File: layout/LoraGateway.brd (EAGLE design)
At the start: 65 x 30 mm, 124 parts, among them J1 RPI-ZERO-HEADER, P2 LTST-C930KGKT, P3 LTST-C930KGKT, U1 SC283, U10 SE2435L, U2 SC560H, U6 SX1257, U7 SX1257, X1 USB2-MICRO, X3 END4825A, X4 END4263A, X5 SMA-KE11

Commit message: Rpi-shield
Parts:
- removed P3: LTST-C930KGKT, LoRa Gateway:LTST-C930KGKT
- removed R19, R22: 100, rcl:R0402
- added C12: 100nF, common:C0402
- added C13: 56pF, rcl:C0402
- added P1, P5, P6, P7, P8: LTST-C930KGKT, LoRa Gateway:LTST-C930KGKT
- added R10, R11, R7, R8, R9: 470, rcl:R0402
- added R3: EXB-N8V101JX, LoRa Gateway:EXB28V
- added R6: 100, rcl:R0402
- added U4: FGPMMOPA6H, LoRa Gateway:FGPMMOPA6H
- added X2: SMA-KE11, LoRa Gateway:J502-ND-142-0711-871/876
- C1, C2, C3, C4: device rcl:C1206 -> common:C1206
- C11, C23, C36, C5, C9: device rcl:C0805 -> common:C0805
- C24, C26, C27, C28, C29, C30, C31, C32, C33, C35, C39, C40, C41, C42, C43, C44, C48, C49, C50, C51, C52, C55, C56, C59, C60, C61, C62, C63, C64, C65, C66, C67, C68, C69, C70, C71, C72, C73, C74: device rcl:C0402 -> common:C0402
- C25, C34, C37, C38, C45, C46, C47, C53, C54, C58, C6: device rcl:C0603 -> common:C0603
- J1: value RPI-ZERO-HEADER -> RPI-HEADER3B; device LoRa Gateway:RPI-ZERO -> LoRa Gateway:RPI
- R16, R17: value 470 -> 100
- R18: value 100 -> 470
- moved L1 154.3 mm to (154.9, 65.7)
- moved C1 154.2 mm to (160.0, 64.0)
- moved U1 153.9 mm to (161.0, 68.0)
- moved C2 153.8 mm to (158.0, 68.0)
- moved C4 153.7 mm to (162.0, 72.0)
- moved C3 153.3 mm to (164.0, 68.0)
- moved L2 152.9 mm to (167.3, 70.3)
- moved P2 138.1 mm to (1.00, -28.0), turned to 0 degrees
- moved R18 123.6 mm to (-1.00, -22.0)
- moved C6 89.8 mm to (142.0, 74.0)
- moved C9 89.3 mm to (142.0, 76.0)
- moved C11 89.3 mm to (142.0, 72.0)
- moved U2 88.6 mm to (145.0, 74.0)
- moved C8 88.6 mm to (147.0, 74.0)
- moved R4 88.5 mm to (148.0, 74.0)
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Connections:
- removed net CLKO_B_32M: R22.2
- removed net GPIO0: U5.58
- removed net GPIO2: U5.56
- removed net GPIO3: U5.55
- removed net N$15 (its old number): P3.1, R17.2
- new net 3V3@1: J1.1
- new net N$10: R3.8, U5.2
- new net N$11: R3.7, U5.3
- new net N$33: R3.5, U5.5
- new net N$42: P1.1, R7.2
- new net N$5: R6.1, U5.39
- new net N$51: U4.11, X2.1
- new net N$66: P6.1, R9.2
- new net N$68: P7.1, R10.2
- new net N$69: P8.1, R11.2
- new net N$7: R11.1, U5.58
- new net N$71: R8.1, U5.55
- new net N$72: R18.2, U4.5
- new net N$73: U4.9
- new net N$74: U4.10
- new net N$75: C12.1, U4.1, U4.2
- new net N$76: P2.1, R18.1
- new net N$8: R9.1, U5.56
- net +5V: now also J1.2, J1.4
- net CLKI: now also R6.2; no longer R18.2
- net CLKO_B: now also R17.2; no longer R19.2, R22.1
- net FEM_EN: now also R16.2; no longer U3.2
- net GND: now also C12.2, C13.2, J1.14, J1.20, J1.25, J1.30, J1.34, J1.39, J1.6, J1.9, P1.2, P5.2, P6.2, P7.2, P8.2, U10.19, U4.12, U4.19, U4.3, U4.8, X2.G@1, X2.G@2, X2.G@3, X2.G@4; no longer P3.2
- net N$12: now also U3.2
- net N$14: now also R3.6, U5.4; no longer P2.1, R16.2
- net N$45: now also P5.1, R8.2; no longer R18.1, U5.39
- net N$58: now also R17.1; no longer R19.1
- net PPS: now also J1.18, U4.13
- net RADIO_RST: now also U5.25
- net RESET: now also J1.22
- net RX_ON: now also R10.1; no longer R17.1
- net SPI_MISO: now also J1.21, R3.2; no longer U5.3
- net SPI_MOSI: now also J1.19, R3.3; no longer U5.4
- net SPI_NSS: now also J1.24, R3.4; no longer U5.5
- net SPI_SCK: now also J1.23, R3.1; no longer U5.2
- net TX_ON: now also R7.1; no longer R16.1
- net VCCINT: now also C13.1, R16.1
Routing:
- net GND: track 0.00 -> 51.0 mm
- net VCCA_B: track 0.00 -> 4.55 mm
- net +5V: track 0.00 -> 4.01 mm
- net N$55: track 0.00 -> 1.70 mm
- net N$54: track 0.00 -> 1.70 mm
- net N$56: track 0.00 -> 1.68 mm
- net N$49: track 0.00 -> 1.45 mm
- net N$32: track 0.00 -> 1.00 mm
- added copper zone on layer 2, net GND
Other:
- board size 65 x 30 mm -> 65 x 56.5 mm

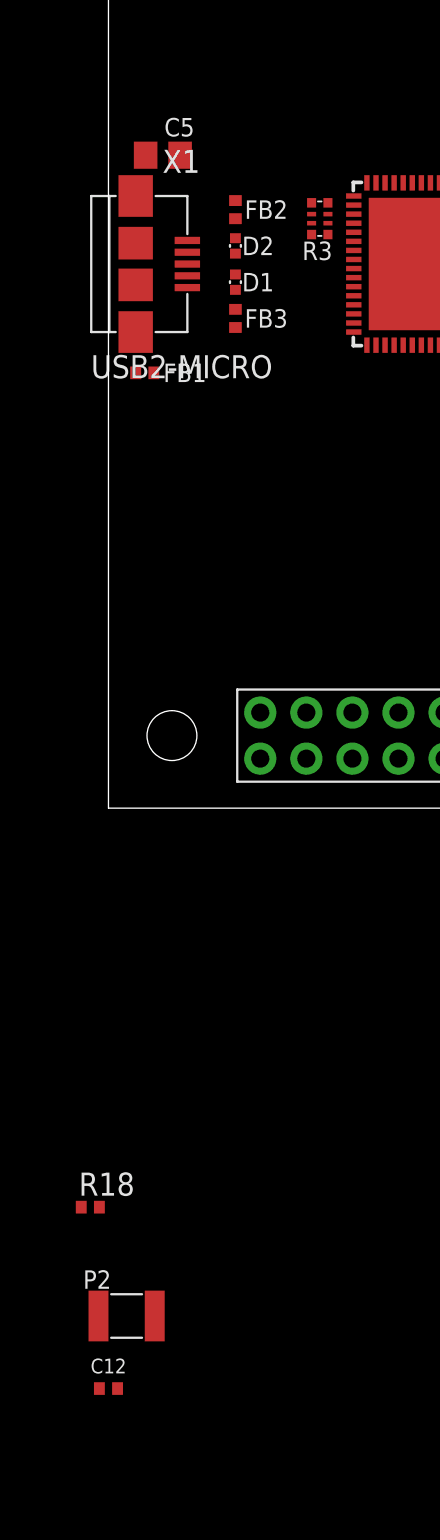
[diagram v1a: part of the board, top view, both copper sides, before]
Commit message: gps modul connected
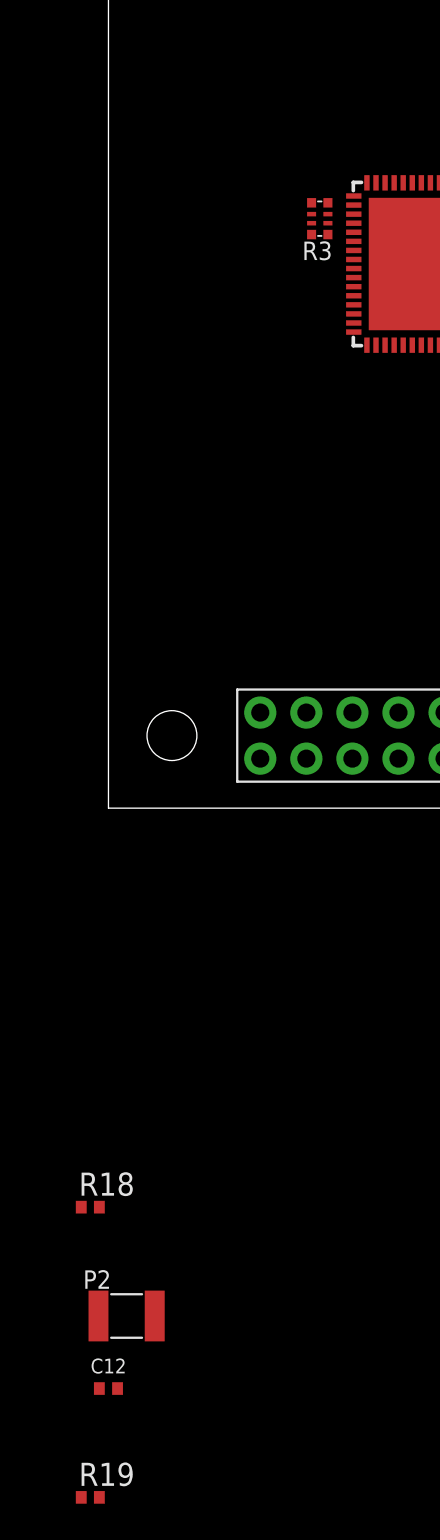
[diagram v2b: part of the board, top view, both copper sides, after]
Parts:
- removed C5: 1µF, common:C0805
- removed D1, D2: RCLAMP0531T, LoRa Gateway:SLP1006P2T
- removed FB1, FB2, FB3: (no value), LoRa Gateway:L0402
- removed X1: USB2-MICRO, LoRa Gateway:USB-2-MICRO
- added R19: 0, rcl:R0402
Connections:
- removed net N$6: D1.1, FB3.1, X1.5
- removed net N$73: U4.9
- removed net N$74: U4.10
- removed net N$9: FB1.2, X1.6, X1.7, X1.8, X1.9
- removed net VBUS: D2.1, FB2.1, X1.1
- new net 3V3@2: J1.17
- new net GPSRX: J1.8, U4.10
- new net GPSTX: J1.10, U4.9
- net +5V: no longer C5.2, FB2.2
- net GND: now also R19.1; no longer C5.1, D1.2, D2.2, FB1.1, FB3.2
- net N$75: now also R19.2

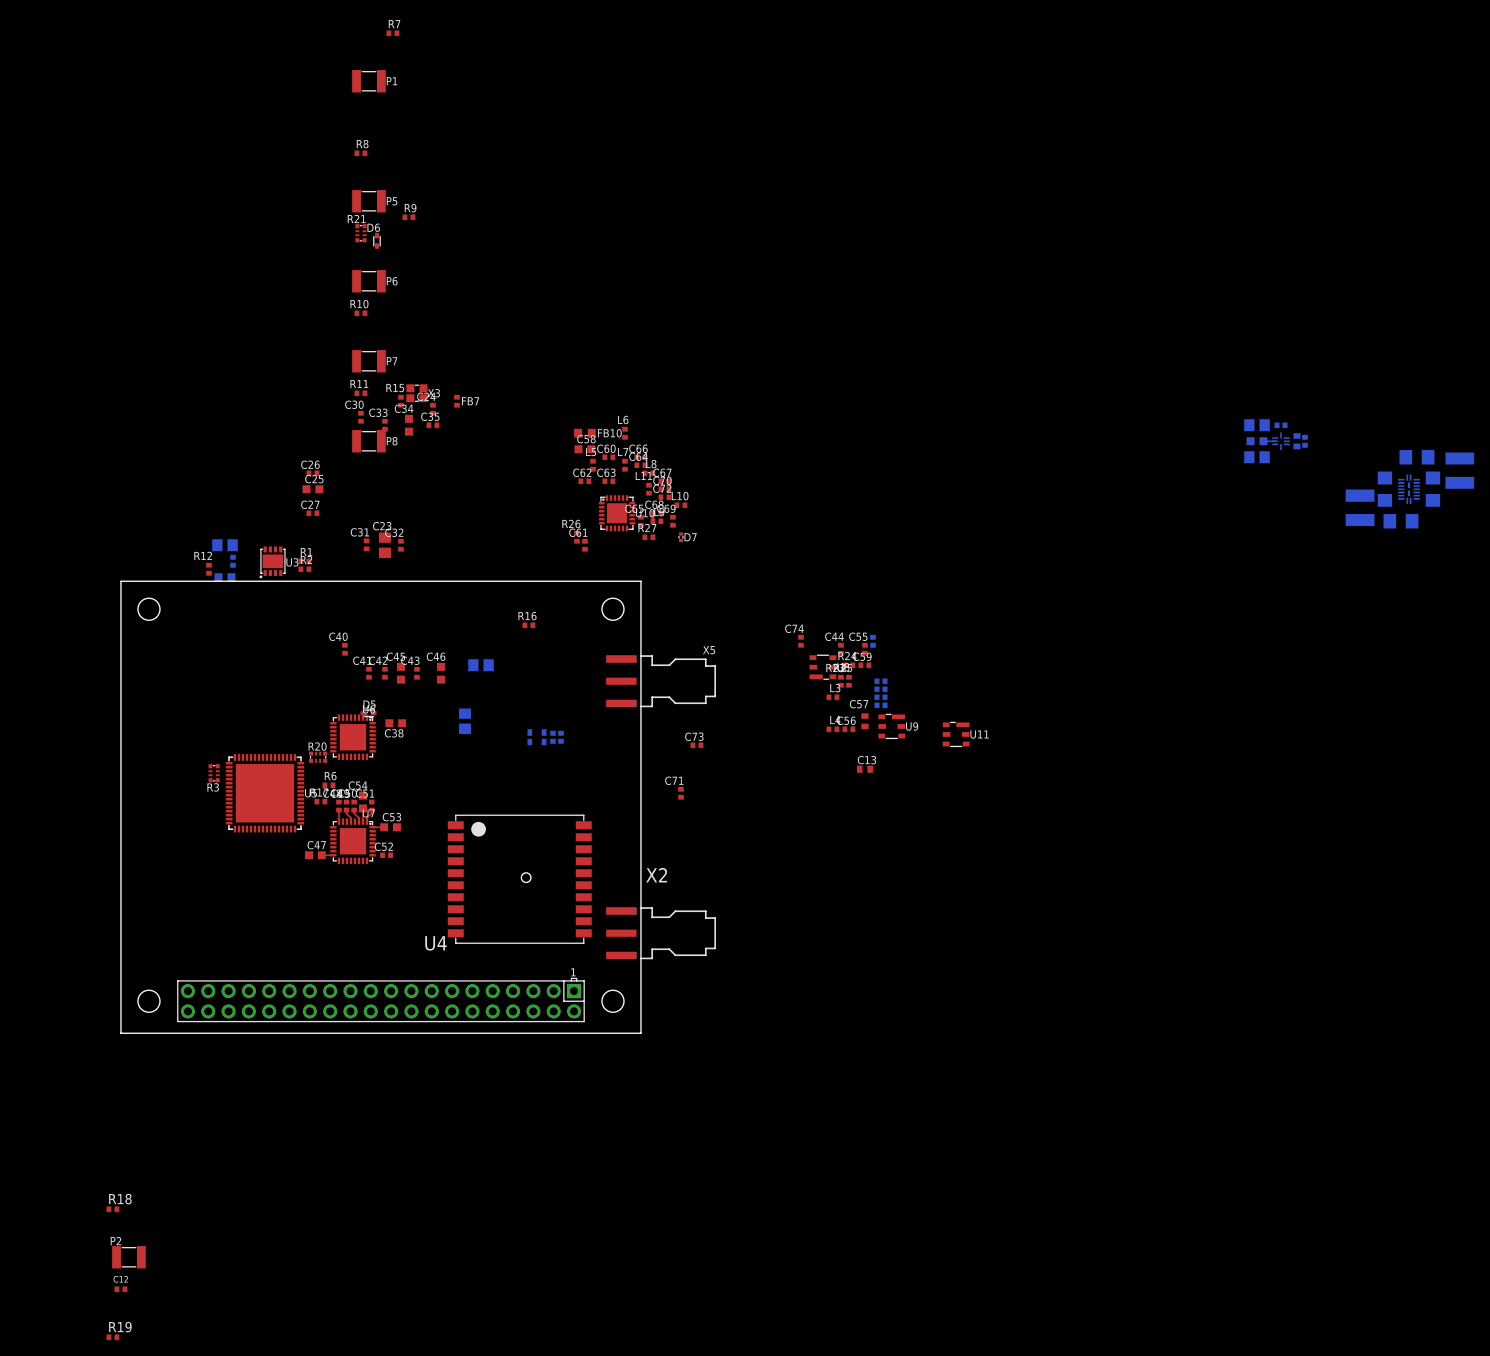
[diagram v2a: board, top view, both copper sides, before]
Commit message: gateway routed
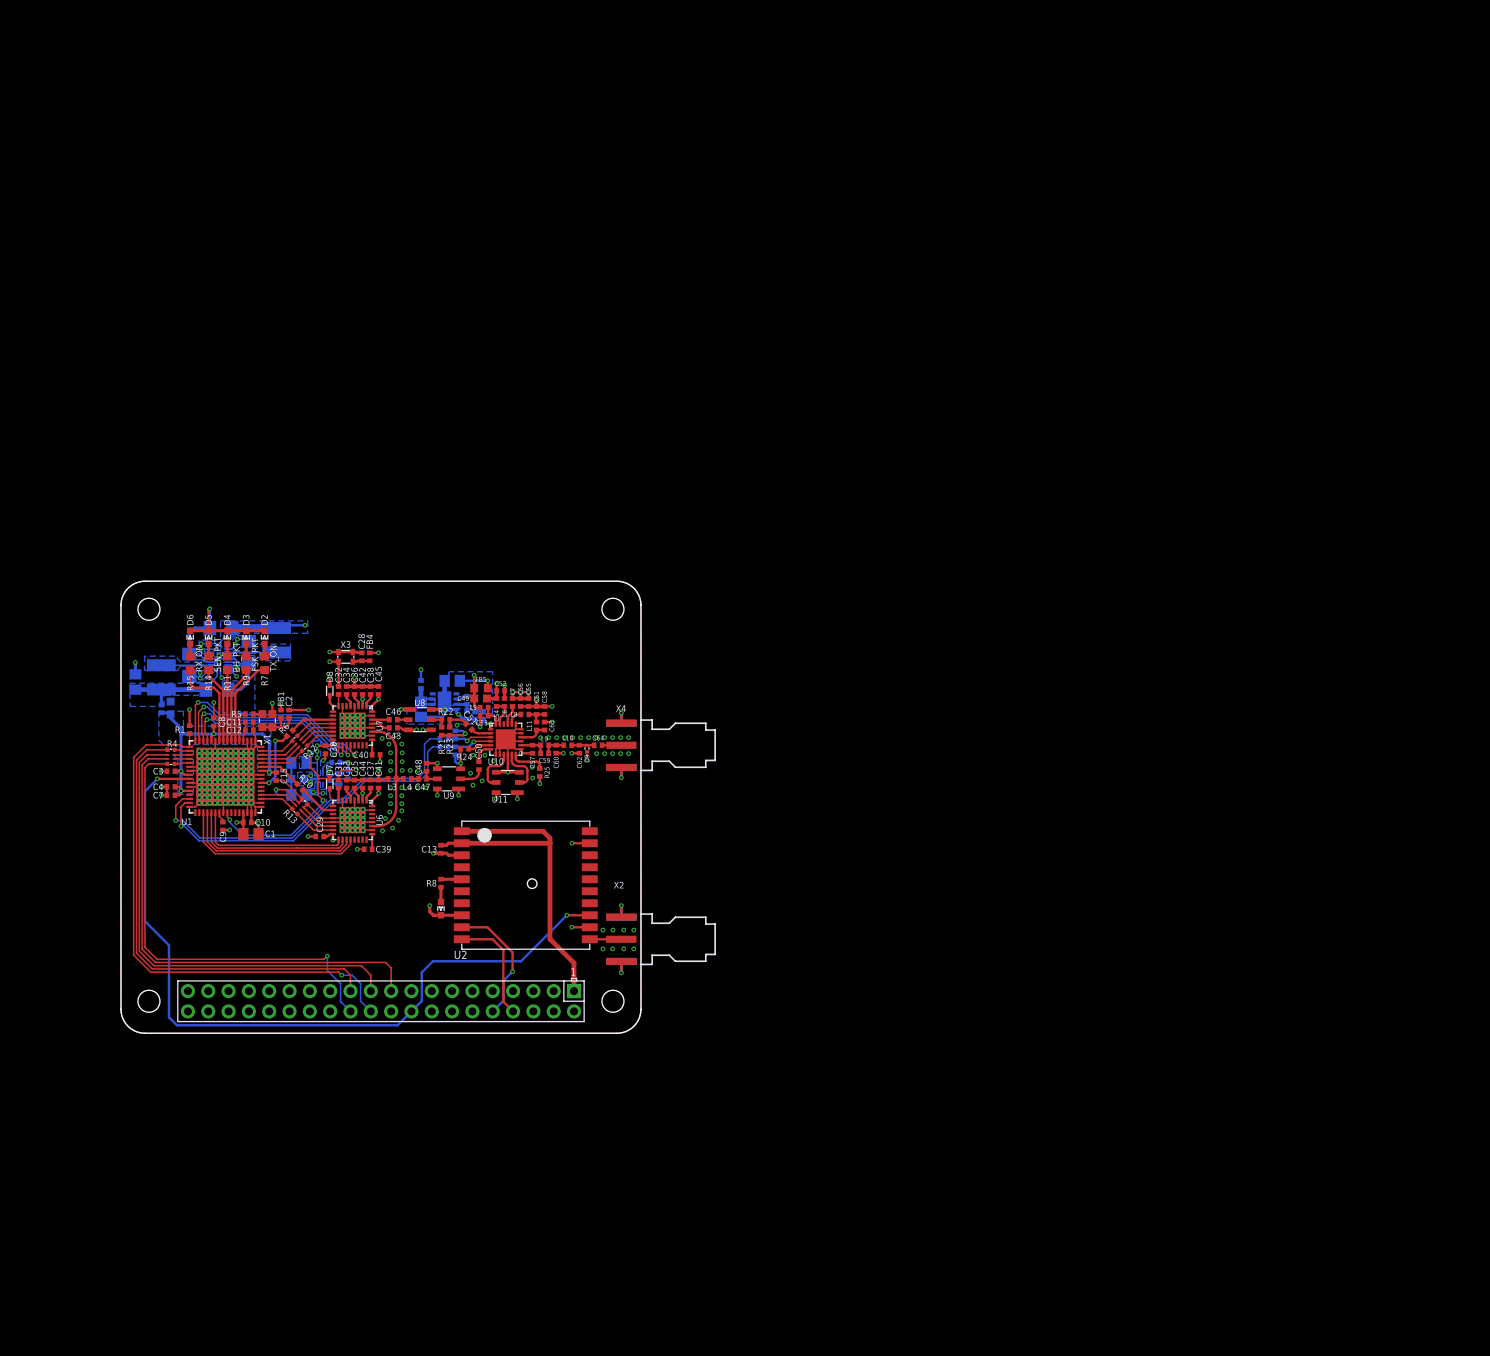
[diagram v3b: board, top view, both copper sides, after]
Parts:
- removed C65, C69: 3.3pF, common:C0402
- removed C66: 33pF, common:C0402
- removed C67: 7.5pF, common:C0402
- removed C68: 1.5pF, common:C0402
- removed C70, C72: 5.1pF, common:C0402
- removed C71: 2.7pF, common:C0402
- removed C73: 56pF, common:C0402
- removed C74: 100nF, common:C0402
- removed FB10: (no value), LoRa Gateway:L0603
- removed FB7, FB8, FB9: (no value), LoRa Gateway:L0402
- removed P1, P2, P5, P6, P7, P8: LTST-C930KGKT, LoRa Gateway:LTST-C930KGKT
- removed R26, R27: 49R9, rcl:R0402
- removed X5: SMA-KE11, LoRa Gateway:J502-ND-142-0711-871/876
- added C14: 10µF, common:C0805
- added C15: 100nF, common:C0402
- added C16: 1µF, common:C0603
- added C17, C21: 10uF, common:C0805
- added C18: 22uF, common:C1206
- added C19: 2.2uF, common:C0603
- added C20: 10uF, common:C1206
- added C22, C5: 56pF, common:C0402
- added D1, D2, D3, D4: LED, common:D0603
- added D8: BAT54XV2T1G, LoRa Gateway:SOD523
- added D9: LXES15AAA1-153, LoRa Gateway:LXES15AAA1-153
- added FB1, FB2, FB3: (no value), LoRa Gateway:L0402
- added FB5: (no value), LoRa Gateway:L0603
- added R22: 18, common:R0402
- added X1: END4825A, LoRa Gateway:2.5X2.0MM
- C1: value 22uF -> 10µF; device common:C1206 -> common:C0805
- C10, C7: value 10uF -> 100nF; device rcl:C0805 -> common:C0402
- C11, C9: value 1uF -> 100nF; device common:C0805 -> common:C0402
- C12, C30, C41, C42: value 100nF -> 1µF
- C13: value 56pF -> 100nF; device rcl:C0402 -> common:C0402
- C2: value 10uF -> 10nF; device common:C1206 -> common:C0402
- C23: value 10µF -> 10uF; device common:C0805 -> common:C1206
- C24: value 10nF -> 100nF; device common:C0402 -> rcl:C0402
- C25: value 1µF -> 1uF; device common:C0603 -> common:C0805
- C26: value 100nF -> 22uF; device common:C0402 -> common:C1206
- C27: value 100nF -> 1uF; device common:C0402 -> common:C0805
- C28: value 56pF -> 100nF
- C29, C44: value 56pF -> 1µF
- C3: value 10uF -> 1µF; device common:C1206 -> common:C0402
- C31, C32: value 100nF -> 1nF
- C34: value 1µF -> 100nF; device common:C0603 -> common:C0402
- C36: value 10µF -> 100nF; device common:C0805 -> common:C0402
- C37, C38: value 1µF -> 10nF; device common:C0603 -> common:C0402
- C4: value 22uF -> 100nF; device common:C1206 -> common:C0402
- C40: value 1nF -> 100nF
- C43: value 10nF -> 56pF
- C45: device common:C0603 -> common:C0402
- C46, C47: value 1µF -> 56pF; device common:C0603 -> common:C0402
- C48: value 1nF -> 5.6pF
- C49: value 100nF -> 4.7µF; device common:C0402 -> common:C0603
- C50: value 100nF -> 56pF
- C51, C60: value 10nF -> 3.3pF
- C52: value 100nF -> 10nF
- C53: value 1µF -> 150pF; device common:C0603 -> common:C0402
- C54: value 1µF -> 22pF; device common:C0603 -> common:C0402
- C55: value 56pF -> 1nF
- C56: value 56pF -> 33pF
- C57: value 5.6pF -> 3.3pF; device rcl:C0402 -> common:C0402
- C58: value 4.7µF -> 7.5pF; device common:C0603 -> common:C0402
- C59: value 3.3pF -> 1.5pF
- C6: value 2.2uF -> 56pF; device common:C0603 -> common:C0402
- C61: value 56pF -> 5.1pF
- C62: value 150pF -> 2.7pF
- C63: value 22pF -> 5.1pF
- C64: value 1nF -> 56pF
- C8: device rcl:C0402 -> common:C0402
- D5, D6: value BAT54XV2T1G -> LED; device LoRa Gateway:SOD523 -> common:D0603
- D7: value LXES15AAA1-153 -> BAT54XV2T1G; device LoRa Gateway:LXES15AAA1-153 -> LoRa Gateway:SOD523
- L10, L11, L3, L4, L5, L6, L7, L8, L9: device LoRa Gateway:L0402 -> common:L0402
- R1: value 16k -> 10k
- R10: value 470 -> 100; device rcl:R0402 -> common:R0402
- R11, R7, R9: device rcl:R0402 -> common:R0603
- R12, R4: value 10k -> EXB-N8V101JX; device rcl:R0402 -> LoRa Gateway:EXB28V
- R13: value 100 -> EXB-N8V101JX; device rcl:R0402 -> LoRa Gateway:EXB28V
- R14: value 100 -> 470; device rcl:R0402 -> common:R0603
- R15: value 0 -> 470; device rcl:R0402 -> common:R0603
- R16, R17: value 100 -> 10k; device rcl:R0402 -> common:R0402
- R18: value 470 -> 16k; device rcl:R0402 -> common:R0402
- R19: value 0 -> 12k; device rcl:R0402 -> common:R0402
- R2: value 12k -> 100; device rcl:R0402 -> common:R0402
- R20, R3: value EXB-N8V101JX -> 100; device LoRa Gateway:EXB28V -> common:R0402
- R21: value EXB-N8V101JX -> 300; device LoRa Gateway:EXB28V -> common:R0402
- R23, R6: device rcl:R0402 -> common:R0402
- R24: value 18 -> 49R9; device rcl:R0402 -> common:R0402
- R25: value 300 -> 49R9; device rcl:R0402 -> common:R0402
- R5: value 10k -> 0; device rcl:R0402 -> common:R0402
- U1: value SC283 -> (none); device LoRa Gateway:2X3MLPQ-W18 -> LoRa Gateway:QFN64-9X9
- U2: value SC560H -> FGPMMOPA6H; device LoRa Gateway:MLPQ-UT8 -> LoRa Gateway:FGPMMOPA6H
- U4: value FGPMMOPA6H -> SC283; device LoRa Gateway:FGPMMOPA6H -> LoRa Gateway:2X3MLPQ-W18
- U5: value (none) -> SC560H; device LoRa Gateway:QFN64-9X9 -> LoRa Gateway:MLPQ-UT8
- X3: value END4825A -> END4263A; device LoRa Gateway:2.5X2.0MM -> LoRa Gateway:2.0X1.6MM
- X4: value END4263A -> SMA-KE11; device LoRa Gateway:2.0X1.6MM -> LoRa Gateway:J502-ND-142-0711-871/876
- moved L2 164.3 mm to (5.05, 44.5), turned to 90 degrees
- moved C3 161.6 mm to (6.25, 32.8), flipped to the top, turned to 180 degrees
- moved C4 161.1 mm to (6.25, 30.8), flipped to the top, turned to 180 degrees
- moved U1 152.3 mm to (13.1, 32.0), flipped to the top, turned to 0 degrees
- moved C1 149.0 mm to (16.2, 24.9), flipped to the top, turned to 0 degrees
- moved R4 147.1 mm to (6.25, 34.5), flipped to the top
- moved C8 139.9 mm to (11.6, 38.9), flipped to the top
- moved C2 139.9 mm to (21.0, 39.9), flipped to the top
- moved C9 138.6 mm to (12.8, 25.9), flipped to the top, turned to 270 degrees
- moved L1 136.5 mm to (19.4, 49.1), turned to 90 degrees
- moved R5 133.9 mm to (16.1, 39.9), flipped to the top, turned to 180 degrees
- moved C11 130.2 mm to (16.1, 38.9), flipped to the top
- moved U2 109.5 mm to (50.6, 18.5), flipped to the top, turned to 0 degrees
- moved C6 107.4 mm to (41.8, 35.3), turned to 270 degrees
- moved R8 91.8 mm to (40.0, 18.8), turned to 90 degrees
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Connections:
- removed net 133M_OUT_EN: X3.1
- removed net 3V3@1: J1.1
- removed net 3V3@2: J1.17
- removed net N$16: C24.1, FB7.2, X3.4
- removed net N$75: C12.1, R19.2, U4.1, U4.2
- new net Q1_VCC: C2.1, FB1.2, X1.1, X1.4
- new net V+: C13.1, J1.1, U2.1, U2.2
- net +5V: now also C19.1, C20.1, C23.1, R16.1, R17.1, U4.1, U4.10, U4.14, U4.15, U4.16, U4.17, U4.5, U4.8, U5.2; no longer C2.1, C3.1, C6.1, R4.1, R5.1, U1.1, U1.10, U1.14, U1.15, U1.16, U1.17, U1.5, U1.8, U2.2
- net CLKHS: now also R5.2, U1.53; no longer R15.2, U5.53
- net CLKI: now also U7.11; no longer U6.11
- net CLKO_B: now also R10.2, U6.10; no longer R17.2, U7.10
- net FEM_EN: now also R20.2; no longer R16.2
- net GND: now also C14.2, C15.2, C16.2, C17.2, C18.2, C19.2, C20.2, C21.2, C22.2, C33.1, C34.1, C35.1, C36.1, C37.1, C38.1, C40.2, C41.2, C42.2, C43.2, C48.2, C49.2, C5.2, C55.2, C56.2, C61.2, D1.C, D2.C, D3.C, D4.C, D5.C, D6.C, D9.2, R1.1, R13.1, R13.2, R13.7, R13.8, R24.1, R25.1, U1.10, U1.11, U1.16, U1.24, U1.30, U1.31, U1.32, U1.33, U1.34, U1.40, U1.41, U1.48, U1.49, U1.50, U1.51, U1.59, U1.EXP, U2.12, U2.19, U2.3, U2.8, U4.13, U4.4, U4.6, U4.7, U4.T1, U4.T2, U5.5, U6.12, U6.13, X1.2, X3.1, X4.G@1, X4.G@2, X4.G@3, X4.G@4; no longer C31.2, C32.2, C33.2, C34.2, C35.2, C36.2, C37.2, C38.2, C41.1, C42.1, C43.1, C46.2, C47.2, C49.1, C50.1, C51.1, C64.2, C65.2, C66.2, C67.2, C69.2, C70.2, C71.2, C72.2, C74.2, D7.2, P1.2, P2.2, P5.2, P6.2, P7.2, P8.2, R12.1, R2.1, R21.1, R21.7, R21.8, R25.2, R26.1, R27.1, U1.12, U1.13, U1.3, U1.4, U1.T1, U1.T2, U2.5, U4.19, U4.8, U5.10, U5.11, U5.16, U5.24, U5.30, U5.31, U5.32, U5.33, U5.34, U5.40, U5.41, U5.48, U5.49, U5.50, U5.51, U5.59, U5.6, U5.7, U5.EXP, U7.12, U7.13, X4.1, X4.2, X5.G@1, X5.G@2, X5.G@3, X5.G@4
- net GPSRX: now also U2.10; no longer U4.10
- net GPSTX: now also U2.9; no longer U4.9
- net IRXD_A: now also R12.5, U7.15; no longer R20.5, U6.15
- net IRXD_B: now also R13.5, U6.15; no longer R21.5, U7.15
- net ITXD_A: now also R12.7, U7.13; no longer R20.7, U6.13
- net LNA_EN: now also C5.1, R2.1; no longer C28.1, R13.1
- net MISO_A: now also U1.62, U7.18; no longer U5.62, U6.18
- net MISO_B: now also U1.21, U6.18; no longer U5.21, U7.18
- net MOSI_A: now also U1.63, U7.19; no longer U5.63, U6.19
- net MOSI_B: now also U1.20, U6.19; no longer U5.20, U7.19
- net N$1: now also U4.2; no longer U1.2
- net N$10: now also R4.8, U1.2; no longer R3.8, U5.2
- net N$11: now also R4.7, U1.3; no longer R3.7, U5.3
- net N$12: now also C17.1, FB3.2; no longer C7.1, FB4.2
- net N$13: now also C40.1, U7.25; no longer C74.1, U6.25
- net N$14: now also R4.6, U1.4; no longer R3.6, U5.4
- net N$15: now also R13.3, U1.36; no longer R21.3, U5.36
- net N$17: now also R5.1, X1.3; no longer R15.1, X3.3
- net N$18: now also C28.1, FB4.2, X3.4; no longer C39.1, FB9.2, X4.4
- net N$19: now also R25.2; no longer R27.2
- net N$2: now also U4.11; no longer U1.11
- net N$22: now also R24.2; no longer R26.2
- net N$23: now also C54.1; no longer C63.1
- net N$24: now also C58.1, C61.1; no longer C67.1, C70.1
- net N$25: now also C53.1; no longer C62.1
- net N$27: now also C59.2, C60.1; no longer C68.2, C69.1
- net N$28: now also R2.2, U1.14; no longer R13.2, U5.14
- net N$29: now also R3.2, U1.15; no longer R14.2, U5.15
- net N$3: now also R18.1, R19.2; no longer R1.1, R2.2
- net N$31: now also C63.1; no longer C72.1
- net N$32: now also C57.1, C59.1; no longer C65.1, C68.1
- net N$33: now also R4.5, U1.5; no longer R3.5, U5.5
- net N$34: now also C62.1, C64.1, D9.1; no longer C71.1, C73.1, D7.1
- net N$35: now also C51.1; no longer C59.1
- net N$36: now also C50.2; no longer C61.2
- net N$37: now also C51.2, R22.1, R23.1; no longer C59.2, R24.1, R25.1
- net N$38: now also C9.1, U1.23; no longer C31.1, U5.23
- net N$39: now also R21.1, R22.2; no longer R23.1, R24.2
- net N$4: now also C24.1, U5.7; no longer C8.1, U2.7
- net N$40: now also C46.2; no longer C55.2
- net N$41: now also C50.1; no longer C61.1
- net N$42: now also D2.A; no longer P1.1
- net N$43: now also C47.2, C48.1; no longer C56.2, C57.1
- net N$44: now also C47.1; no longer C56.1
- net N$45: now also D3.A, R9.2; no longer P5.1, R8.2
- net N$46: now also C46.1, U7.30; no longer C55.1, U6.30
- net N$47: now also C39.1, U6.25; no longer C52.1, U7.25
- net N$48: now also D7.C, U6.9; no longer D6.C, U7.9
- net N$49: now also C31.1, U6.8; no longer C48.1, U7.8
- net N$5: now also U1.39; no longer U5.39
- net N$50: now also R13.4, U1.35; no longer R21.4, U5.35
- net N$51: now also U2.11; no longer U4.11
- net N$52: now also C32.1, U7.8; no longer C40.1, U6.8
- net N$53: now also C38.2, U7.1; no longer C43.2, U6.1
- net N$54: now also C37.2, U6.1; no longer C51.2, U7.1
- net N$55: now also C35.2, U6.3; no longer C50.2, U7.3
- net N$56: now also C33.2, U6.5; no longer C49.2, U7.5
- net N$57: now also C36.2, U7.3; no longer C42.2, U6.3
- net N$58: now also R10.1, U1.43; no longer R17.1, U5.43
- net N$59: now also R12.4, U1.44; no longer R20.4, U5.44
- net N$60: now also R12.3, U1.45; no longer R20.3, U5.45
- net N$61: now also R12.2, U1.46; no longer R20.2, U5.46
- net N$62: now also R12.1, U1.47; no longer R20.1, U5.47
- net N$63: now also C34.2, U7.5; no longer C41.2, U6.5
- net N$64: now also C43.1, U7.29; no longer C44.1, U6.29
- net N$65: now also C64.2, X4.1; no longer C73.2, X5.1
- net N$66: now also D4.A, R11.2; no longer P6.1, R9.2
- net N$67: now also C11.1, C12.1, U1.52; no longer C33.1, C34.1, U5.52
- net N$68: now also D5.A, R14.2; no longer P7.1, R10.2
- net N$69: now also D6.A, R15.2; no longer P8.1, R11.2
- net N$7: now also R15.1, U1.58; no longer R11.1, U5.58
- net N$70: now also D8.C, U7.9; no longer D5.C, U6.9
- net N$71: now also R9.1, U1.55; no longer R8.1, U5.55
- net N$72: now also R8.2, U2.5; no longer R18.2, U4.5
- net N$76: now also D1.A, R8.1; no longer P2.1, R18.1
- net N$8: now also R11.1, U1.56; no longer R9.1, U5.56
- net NSS_A: now also U1.64, U7.20; no longer U5.64, U6.20
- net NSS_B: now also U1.19, U6.20; no longer U5.19, U7.20
- net PA_EN: now also C6.1, R3.1; no longer C29.1, R14.1
- net PPS: now also U1.9, U2.13; no longer U4.13, U5.9
- net QRXD_A: now also R12.6, U7.14; no longer R20.6, U6.14
- net QRXD_B: now also R13.6, U6.14; no longer R21.6, U7.14
- net QTXD_A: now also R12.8, U7.12; no longer R20.8, U6.12
- net RADIO_EN_A: now also R16.2, U5.6; no longer R4.2, U2.6
- net RADIO_EN_B: now also R17.2, U5.4; no longer R5.2, U2.4
- net RADIO_RST: now also D7.A, D8.A, U1.25; no longer D5.A, D6.A, U5.25
- net RESET: now also R1.2, U1.1; no longer R12.2, U5.1
- net RX_ON: now also R14.1, U1.57; no longer R10.1, U5.57
- net SCK_A: now also U1.61, U7.17; no longer U5.61, U6.17
- net SCK_B: now also U1.22, U6.17; no longer U5.22, U7.17
- net SPI_MISO: now also R4.2; no longer R3.2
- net SPI_MOSI: now also R4.3; no longer R3.3
- net SPI_NSS: now also R4.4; no longer R3.4
- net SPI_SCK: now also R4.1; no longer R3.1
- net TX_ON: now also U1.54; no longer U5.54
- net VCC: now also C14.1, C26.1, FB2.1, U4.9; no longer C36.1, C4.1, FB8.1, U1.9
- net VCCA_A: now also C25.1, C30.1, C42.1, C52.1, FB4.1, U5.3, U7.16, U7.2, U7.32; no longer C38.1, C46.1, C60.1, C9.1, FB9.1, U2.3, U6.16, U6.2, U6.32
- net VCCA_B: now also C27.1, C29.1, C41.1, C44.1, U5.1, U6.16, U6.2, U6.32; no longer C11.1, C47.1, C53.1, C54.1, U2.1, U7.16, U7.2, U7.32
- net VCCDIG18: now also C15.1, C16.1, C3.1, C4.1, C7.1, C8.1, FB2.2, U1.12, U1.42, U1.60, U1.8; no longer C25.1, C26.1, C27.1, C30.1, C35.1, C37.1, FB8.2, U5.12, U5.42, U5.60, U5.8
- net VCCDIG33: now also C10.1, C18.1, FB1.1, FB3.1, U1.29, U4.18; no longer C23.1, C32.1, FB4.1, FB7.1, U1.18, U5.29
- net VCCINT: now also C21.1, C22.1, FB5.1, R18.2, R20.1; no longer C10.1, C13.1, FB10.1, R1.2, R16.1
- net VCC_FEM: now also C49.1, C55.1, C56.1, FB5.2; no longer C58.1, C64.1, C66.1, FB10.2
- net XTL_OUT: now also C31.2, C32.2, X3.3; no longer C40.2, C48.2, X4.3
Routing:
- net GND: track 51.0 -> 235.3 mm, vias 0 -> 286
- net +5V: track 4.01 -> 164.4 mm, vias 0 -> 11
- net PPS: track 0.00 -> 96.5 mm, vias 0 -> 2
- net RESET: track 0.00 -> 67.9 mm, vias 0 -> 1
- net VCCDIG33: track 0.00 -> 67.1 mm, vias 0 -> 4
- net SPI_MOSI: track 0.00 -> 61.5 mm
- net SPI_MISO: track 0.00 -> 59.7 mm
- net SPI_SCK: track 0.00 -> 58.4 mm
- net SPI_NSS: track 0.00 -> 57.2 mm, vias 0 -> 1
- net VCCA_A: track 0.00 -> 48.8 mm, vias 0 -> 7
- net V+: track 0.00 -> 46.1 mm
- net N$28: track 0.00 -> 45.0 mm, vias 0 -> 1
- net N$29: track 0.00 -> 43.2 mm, vias 0 -> 1
- net VCCDIG18: track 0.00 -> 36.0 mm, vias 0 -> 4
- net RADIO_RST: track 0.00 -> 35.2 mm, vias 0 -> 4
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- added copper zone on layer 15, net +5V
- added copper zone on layer 16, net +5V
- added copper zone on layer 1, net GND
- added copper zone on layer 16, net GND
- added copper zone on layer 16, net N$1
- added copper zone on layer 16, net N$12
- added copper zone on layer 16, net N$2
- added copper zone on layer 1, net N$6
- added copper zone on layer 16, net N$9
- added copper zone on layer 16, net VCC
- added copper zone on layer 16, net VCCA_A
- added copper zone on layer 16, net VCCA_B
- added copper zone on layer 16, net VCCDIG18
- added copper zone on layer 15, net VCCDIG33
- added copper zone on layer 16, net VCCDIG33
- added copper zone on layer 16, net VCCINT
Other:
- outline, holes or cut-outs redrawn
- board text added: "BH_PKT"
- board text added: "FSK_PKT"
- board text added: "RX_ON"
- board text added: "SEN_PKT"
- board text added: "TX_ON"
